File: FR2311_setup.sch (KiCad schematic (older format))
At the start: 10 parts

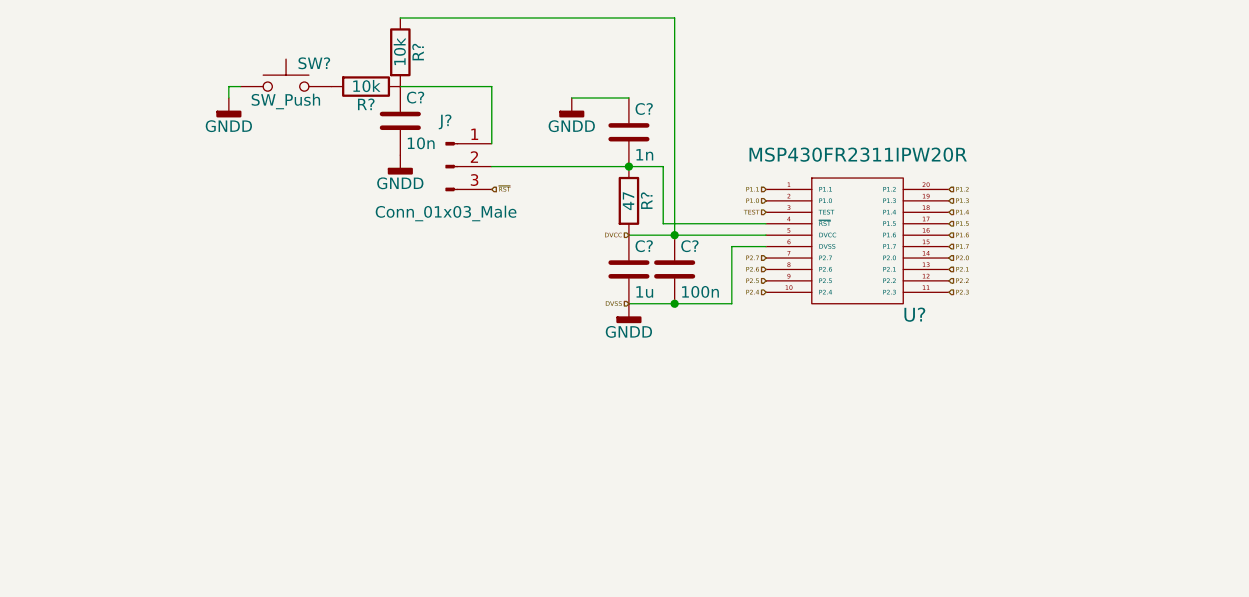
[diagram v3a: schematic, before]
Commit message: Finished Rev1 schematic and assigned most footprints
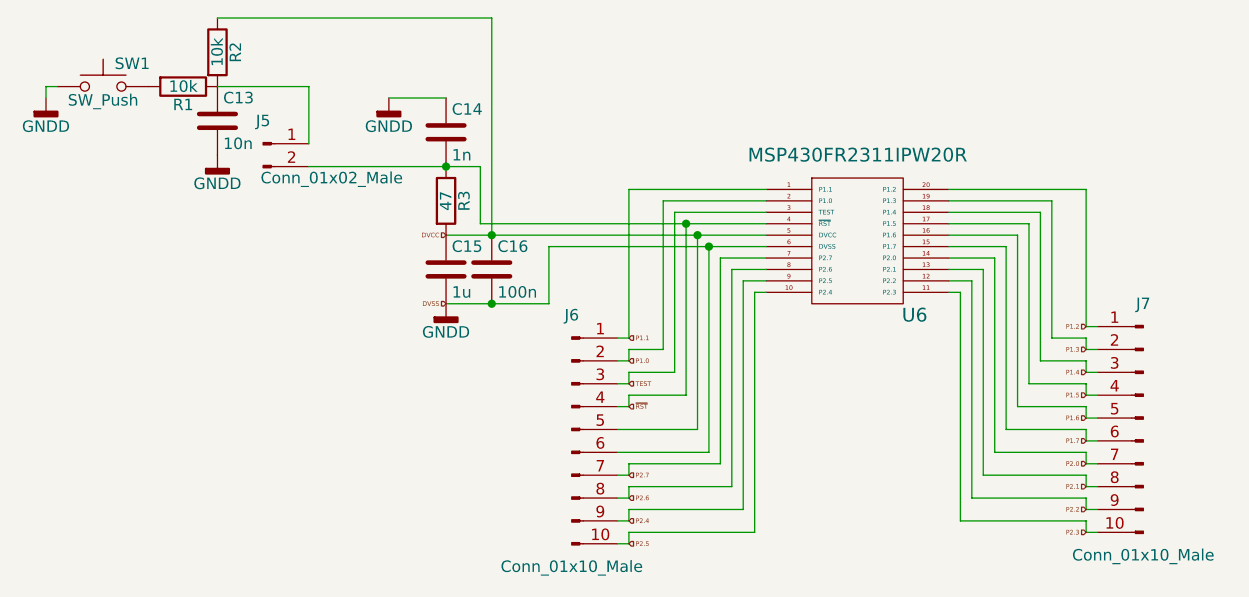
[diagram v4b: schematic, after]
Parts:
- removed J?: Conn_01x03_Male, symbol Conn_01x03_Male
- added J5: Conn_01x02_Male, Pin_Headers:Pin_Header_Angled_1x02_Pitch2.54mm, symbol Conn_01x02_Male
- added J6, J7: Conn_01x10_Male, Pin_Headers:Pin_Header_Angled_1x10_Pitch2.54mm, symbol Conn_01x10_Male
- C13, C14, C15, C16: renamed from C?; footprint (none) -> Capacitors_SMD:C_0603
- R1, R2, R3: renamed from R?; footprint (none) -> Resistors_SMD:R_0603
- SW1: renamed from SW?; footprint (none) -> MyLib:FSM2JSMAATR
- U6: renamed from U?; footprint (none) -> Housings_SSOP:TSSOP-20_4.4x6.5mm_Pitch0.65mm
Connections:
- net DVCC: now also J6.5 (Pin_5)
- net GNDD: now also J6.6 (Pin_6)
- net P1.0: now also J6.2 (Pin_2)
- net P1.1: now also J6.1 (Pin_1)
- net P1.2: now also J7.1 (Pin_1)
- net P1.3: now also J7.2 (Pin_2)
- net P1.4: now also J7.3 (Pin_3)
- net P1.5: now also J7.4 (Pin_4)
- net P1.6: now also J7.5 (Pin_5)
- net P1.7: now also J7.6 (Pin_6)
- net P2.0: now also J7.7 (Pin_7)
- net P2.1: now also J7.8 (Pin_8)
- net P2.2: now also J7.9 (Pin_9)
- net P2.3: now also J7.10 (Pin_10)
- net P2.4: now also U6.9 (P2.5), J6.9 (Pin_9); no longer U6.10 (P2.4)
- net P2.5: now also U6.10 (P2.4), J6.10 (Pin_10); no longer U6.9 (P2.5)
- net P2.6: now also J6.8 (Pin_8)
- net P2.7: now also J6.7 (Pin_7)
- net TEST: now also J6.3 (Pin_3)
- net ~RST: now also C14.2, R3.1, U6.4 (~RST), J5.2 (Pin_2), J6.4 (Pin_4)
- net at C13.1, R1.1, R2.2: now also J5.1 (Pin_1)
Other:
- moved on the sheet: C13, C14, C15, C16, R1, R2, R3, SW1

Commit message: Halfway through layout. Started libraries.
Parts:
- J5: footprint Pin_Headers:Pin_Header_Angled_1x02_Pitch2.54mm -> Pin_Headers:Pin_Header_Straight_1x02_Pitch2.54mm
- J6, J7: footprint Pin_Headers:Pin_Header_Angled_1x10_Pitch2.54mm -> Pin_Headers:Pin_Header_Straight_1x10_Pitch2.54mm
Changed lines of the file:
@@
 EESchema Schematic File Version 2
-LIBS:MyLib
+LIBS:74xgxx
+LIBS:74xx
 LIBS:ac-dc
+LIBS:actel
 LIBS:adc-dac
+LIBS:allegro
 LIBS:Altera
 LIBS:analog_devices
@@
 LIBS:atmel
 LIBS:audio
-LIBS:Battery_Management
+LIBS:battery_management
 LIBS:bbd
 LIBS:bosch
 LIBS:brooktre
-LIBS:Connector
+LIBS:cmos_ieee
+LIBS:cmos4000
+LIBS:conn
 LIBS:contrib
 LIBS:cypress
@@
 LIBS:device
 LIBS:digital-audio
-LIBS:Diode
-LIBS:Display
-LIBS:driver_gate
+LIBS:diode
+LIBS:display
 LIBS:dsp
-LIBS:DSP_Microchip_DSPIC33
 LIBS:elec-unifil
 LIBS:ESD_Protection
-LIBS:Espressif
-LIBS:FPGA_Actel
 LIBS:ftdi
 LIBS:gennum
-LIBS:Graphic
+LIBS:graphic_symbols
 LIBS:hc11
 LIBS:infineon
@@
 LIBS:ir
 LIBS:Lattice
-LIBS:LED
+LIBS:leds
 LIBS:LEM
 LIBS:linear
-LIBS:Logic_74xgxx
-LIBS:Logic_74xx
-LIBS:Logic_CMOS_4000
-LIBS:Logic_CMOS_IEEE
 LIBS:logic_programmable
-LIBS:Logic_TTL_IEEE
 LIBS:maxim
-LIBS:MCU_Microchip_PIC10
-LIBS:MCU_Microchip_PIC12
-LIBS:MCU_Microchip_PIC16
-LIBS:MCU_Microchip_PIC18
-LIBS:MCU_Microchip_PIC24
-LIBS:MCU_Microchip_PIC32
-LIBS:MCU_NXP_Kinetis
-LIBS:MCU_NXP_LPC
-LIBS:MCU_NXP_S08
-LIBS:MCU_ST_STM8
-LIBS:MCU_ST_STM32
-LIBS:MCU_Texas_MSP430
-LIBS:Mechanical
+LIBS:mechanical
 LIBS:memory
 LIBS:microchip
+LIBS:microchip_dspic33dsc
+LIBS:microchip_pic10mcu
+LIBS:microchip_pic12mcu
+LIBS:microchip_pic16mcu
+LIBS:microchip_pic18mcu
+LIBS:microchip_pic24mcu
+LIBS:microchip_pic32mcu
 LIBS:microcontrollers
 LIBS:modules
-LIBS:Motor
 LIBS:motor_drivers
 LIBS:motorola
+LIBS:motors
+LIBS:msp430
 LIBS:nordicsemi
 LIBS:nxp
+LIBS:nxp_armmcu
 LIBS:onsemi
 LIBS:opto
@@
 LIBS:references
 LIBS:regul
-LIBS:Relay
+LIBS:relays
 LIBS:rfcom
 LIBS:RFSolutions
-LIBS:Sensor_Current
 LIBS:sensors
 LIBS:silabs
 LIBS:siliconi
+LIBS:stm8
+LIBS:stm32
 LIBS:supertex
-LIBS:Switch
+LIBS:switches
 LIBS:texas
-LIBS:Transformer
-LIBS:Transistor
+LIBS:transf
+LIBS:transistors
 LIBS:triac_thyristor
-LIBS:Valve
+LIBS:ttl_ieee
+LIBS:valves
 LIBS:video
 LIBS:wiznet
@@
 LIBS:zetex
 LIBS:Zilog
-LIBS:74xgxx
-LIBS:74xx
-LIBS:actel
-LIBS:cmos_ieee
-LIBS:cmos4000
-LIBS:conn
-LIBS:logo
-LIBS:microchip_dspic33dsc
-LIBS:microchip_pic10mcu
-LIBS:microchip_pic12mcu
-LIBS:microchip_pic16mcu
-LIBS:microchip_pic18mcu
-LIBS:microchip_pic32mcu
-LIBS:msp430
-LIBS:nxp_armmcu
-LIBS:relays
-LIBS:stm8
-LIBS:stm32
-LIBS:switches
-LIBS:transf
-LIBS:transistors
-LIBS:ttl_ieee
-LIBS:valves
+LIBS:MyLib
 LIBS:Modulin-cache
 EELAYER 25 0
@@
 $Descr A4 11693 8268
 encoding utf-8
-Sheet 2 6
+Sheet 3 6
 Title ""
 Date ""
@@
 $EndComp
 $Comp
-L GNDD #PWR019
+L GNDD #PWR025
 U 1 1 5A14853F
 P 4650 4050
-AR Path="/5A1481F4/5A14853F" Ref="#PWR019"  Part="1"
-AR Path="/5A150559/5A14853F" Ref="#PWR023"  Part="1"
-F 0 "#PWR019" H 4650 3800 50  0001 C CNN
+AR Path="/5A1481F4/5A14853F" Ref="#PWR025"  Part="1"
+AR Path="/5A150559/5A14853F" Ref="#PWR029"  Part="1"
+F 0 "#PWR025" H 4650 3800 50  0001 C CNN
 F 1 "GNDD" H 4650 3925 50  0000 C CNN
 F 2 "" H 4650 4050 50  0001 C CNN
@@
 $EndComp
 $Comp
-L GNDD #PWR020
+L GNDD #PWR026
 U 1 1 5A148988
 P 4400 3150
-AR Path="/5A1481F4/5A148988" Ref="#PWR020"  Part="1"
-AR Path="/5A150559/5A148988" Ref="#PWR024"  Part="1"
-F 0 "#PWR020" H 4400 2900 50  0001 C CNN
+AR Path="/5A1481F4/5A148988" Ref="#PWR026"  Part="1"
+AR Path="/5A150559/5A148988" Ref="#PWR030"  Part="1"
+F 0 "#PWR026" H 4400 2900 50  0001 C CNN
 F 1 "GNDD" H 4400 3025 50  0000 C CNN
 F 2 "" H 4400 3150 50  0001 C CNN
@@
 $EndComp
 $Comp
-L GNDD #PWR021
+L GNDD #PWR027
 U 1 1 5A14986C
 P 2900 3150
-AR Path="/5A1481F4/5A14986C" Ref="#PWR021"  Part="1"
-AR Path="/5A150559/5A14986C" Ref="#PWR025"  Part="1"
-F 0 "#PWR021" H 2900 2900 50  0001 C CNN
+AR Path="/5A1481F4/5A14986C" Ref="#PWR027"  Part="1"
+AR Path="/5A150559/5A14986C" Ref="#PWR031"  Part="1"
+F 0 "#PWR027" H 2900 2900 50  0001 C CNN
 F 1 "GNDD" H 2900 3025 50  0000 C CNN
 F 2 "" H 2900 3150 50  0001 C CNN
@@
 $EndComp
 $Comp
-L GNDD #PWR022
+L GNDD #PWR028
 U 1 1 5A149872
 P 3650 3400
-AR Path="/5A1481F4/5A149872" Ref="#PWR022"  Part="1"
-AR Path="/5A150559/5A149872" Ref="#PWR026"  Part="1"
-F 0 "#PWR022" H 3650 3150 50  0001 C CNN
+AR Path="/5A1481F4/5A149872" Ref="#PWR028"  Part="1"
+AR Path="/5A150559/5A149872" Ref="#PWR032"  Part="1"
+F 0 "#PWR028" H 3650 3150 50  0001 C CNN
 F 1 "GNDD" H 3650 3275 50  0000 C CNN
 F 2 "" H 3650 3400 50  0001 C CNN
@@
 F 0 "J5" H 3850 3450 50  0000 C CNN
 F 1 "Conn_01x02_Male" H 4150 3200 50  0000 C CNN
-F 2 "Pin_Headers:Pin_Header_Angled_1x02_Pitch2.54mm" H 3850 3350 50  0001 C CNN
+F 2 "Pin_Headers:Pin_Header_Straight_1x02_Pitch2.54mm" H 3850 3350 50  0001 C CNN
 F 3 "" H 3850 3350 50  0001 C CNN
 	1    3850 3350
@@
 F 0 "J6" H 5200 5100 50  0000 C CNN
 F 1 "Conn_01x10_Male" H 5200 4000 50  0000 C CNN
-F 2 "Pin_Headers:Pin_Header_Angled_1x10_Pitch2.54mm" H 5200 4600 50  0001 C CNN
+F 2 "Pin_Headers:Pin_Header_Straight_1x10_Pitch2.54mm" H 5200 4600 50  0001 C CNN
 F 3 "" H 5200 4600 50  0001 C CNN
 	1    5200 4600
@@
 F 0 "J7" H 7700 5050 50  0000 C CNN
 F 1 "Conn_01x10_Male" H 7700 3950 50  0000 C CNN
-F 2 "Pin_Headers:Pin_Header_Angled_1x10_Pitch2.54mm" H 7700 4550 50  0001 C CNN
+F 2 "Pin_Headers:Pin_Header_Straight_1x10_Pitch2.54mm" H 7700 4550 50  0001 C CNN
 F 3 "" H 7700 4550 50  0001 C CNN
 	1    7700 4550
